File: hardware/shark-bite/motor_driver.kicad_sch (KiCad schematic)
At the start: 35 parts, among them J4 Conn_01x02_Male-Connector, U10 IRFH7440TRPBF, U11 IRFH7440TRPBF, U16 IRFH7440TRPBF, U17 IRFH7440TRPBF, U22 AOZ1282CI, U25 GD32E230G6U6TR, U28 FD6288Q, U4 IRFH7440TRPBF, U7 IRFH7440TRPBF

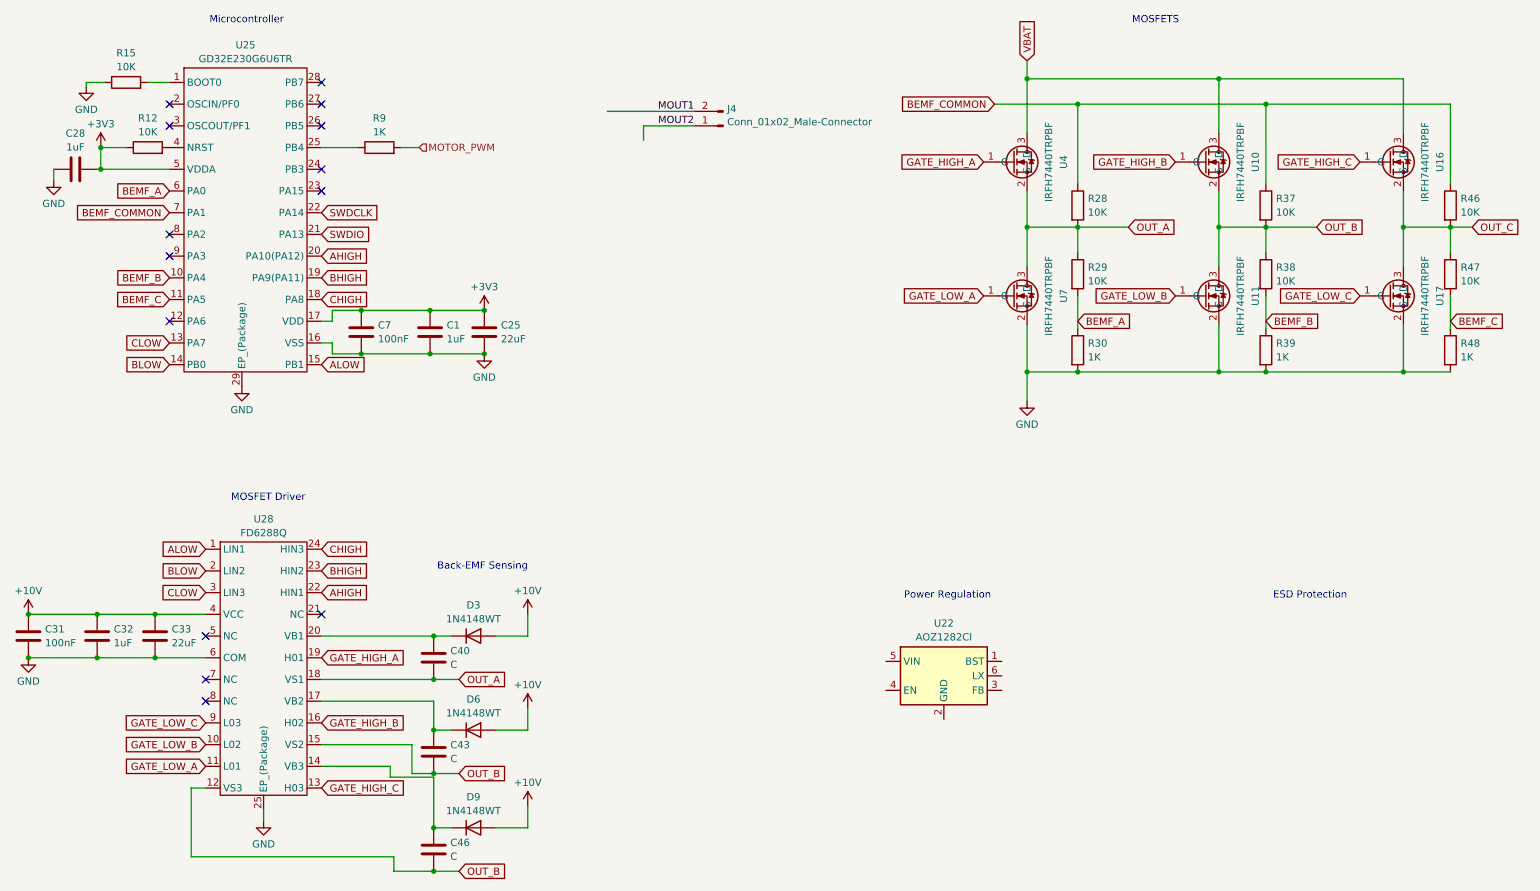
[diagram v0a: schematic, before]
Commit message: Added TVS Diodes
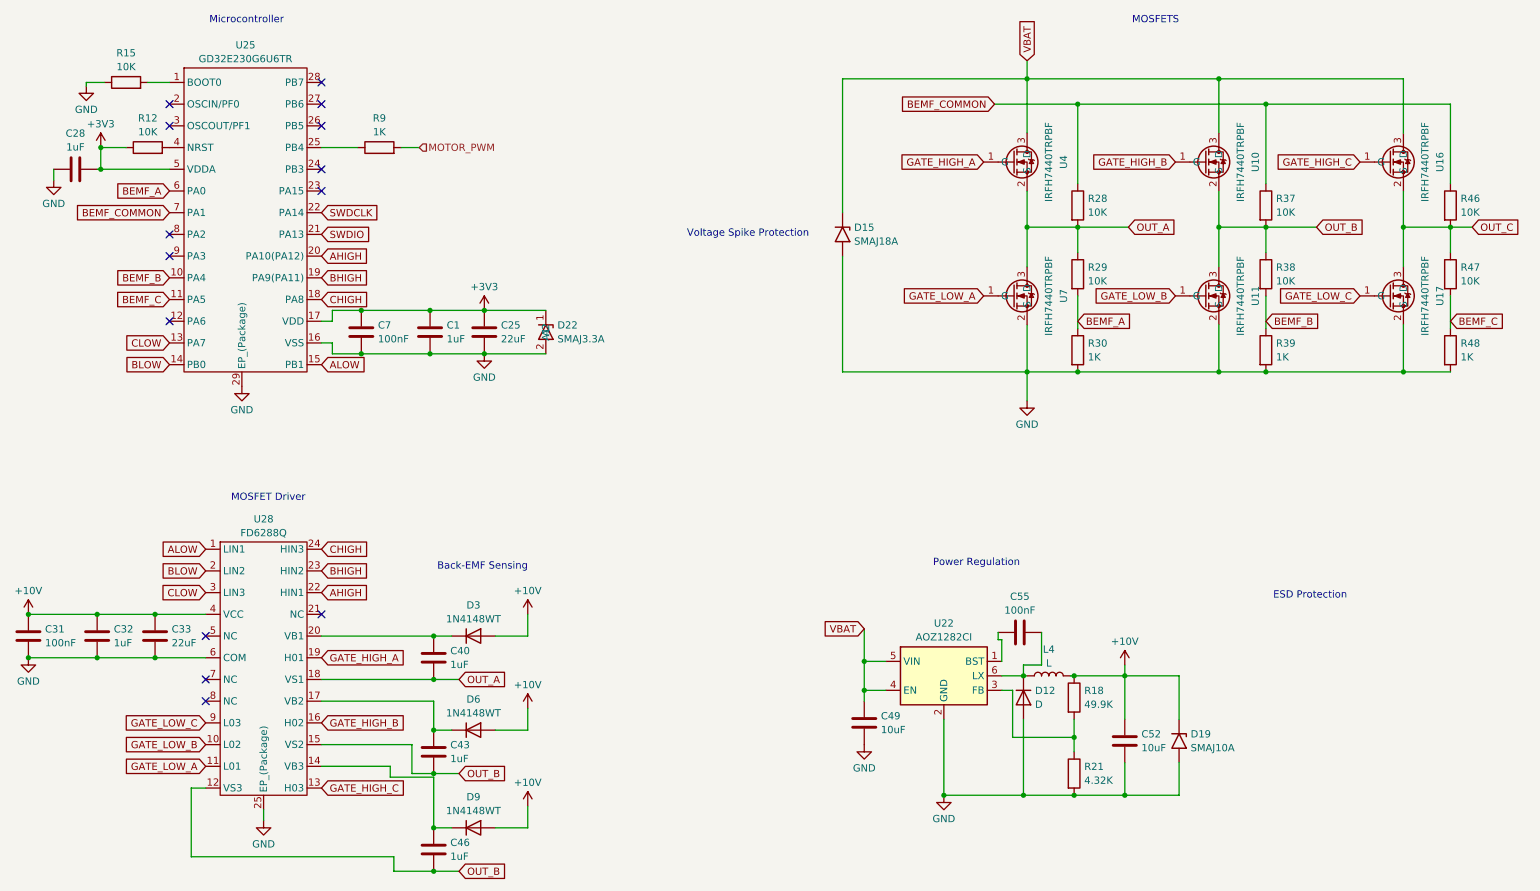
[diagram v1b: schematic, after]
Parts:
- removed J4: Conn_01x02_Male-Connector, malenki-nano:PinHeader_1x02_P2.54mm_BIG1, symbol malenki-nano-rescue:Conn_01x02_Male-Connector
- added C49, C52: 10uF, symbol Device:C
- added C55: 100nF, symbol Device:C
- added D12: D, symbol Device:D
- added D15: SMAJ18A, Diode_SMD:D_SMA, symbol Diode:SMAJ18A
- added D19: SMAJ10A, Diode_SMD:D_SMA, symbol Diode:SMAJ10A
- added D22: SMAJ3.3A, Diode_SMD:D_SMA, symbol Sharkbite:BORN_SMAJ3.3A
- added L4: L, symbol Device:L
- added R18: 49.9K, symbol Device:R
- added R21: 4.32K, symbol Device:R
- C40, C43, C46: value C -> 1uF
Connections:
- net +10V: now also C52.1, D19.1 (A1), L4.2, R18.1
- net +3V3: now also D22.1 (A1)
- net GND: now also U22.2 (GND), C49.2, C52.2, D12.2 (A), D15.2 (A2), D19.2 (A2), D22.2 (A2), R21.2
- net VBAT: now also U22.4 (EN), U22.5 (VIN), C49.1, D15.1 (A1)
- net at U22.1 (BST): now also C55.1
- net at U22.3 (FB): now also R18.2, R21.1
- net at U22.6 (LX): now also C55.2, D12.1 (K), L4.1
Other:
- note added: "Voltage Spike Protection"

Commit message: Removed Extra Diodes
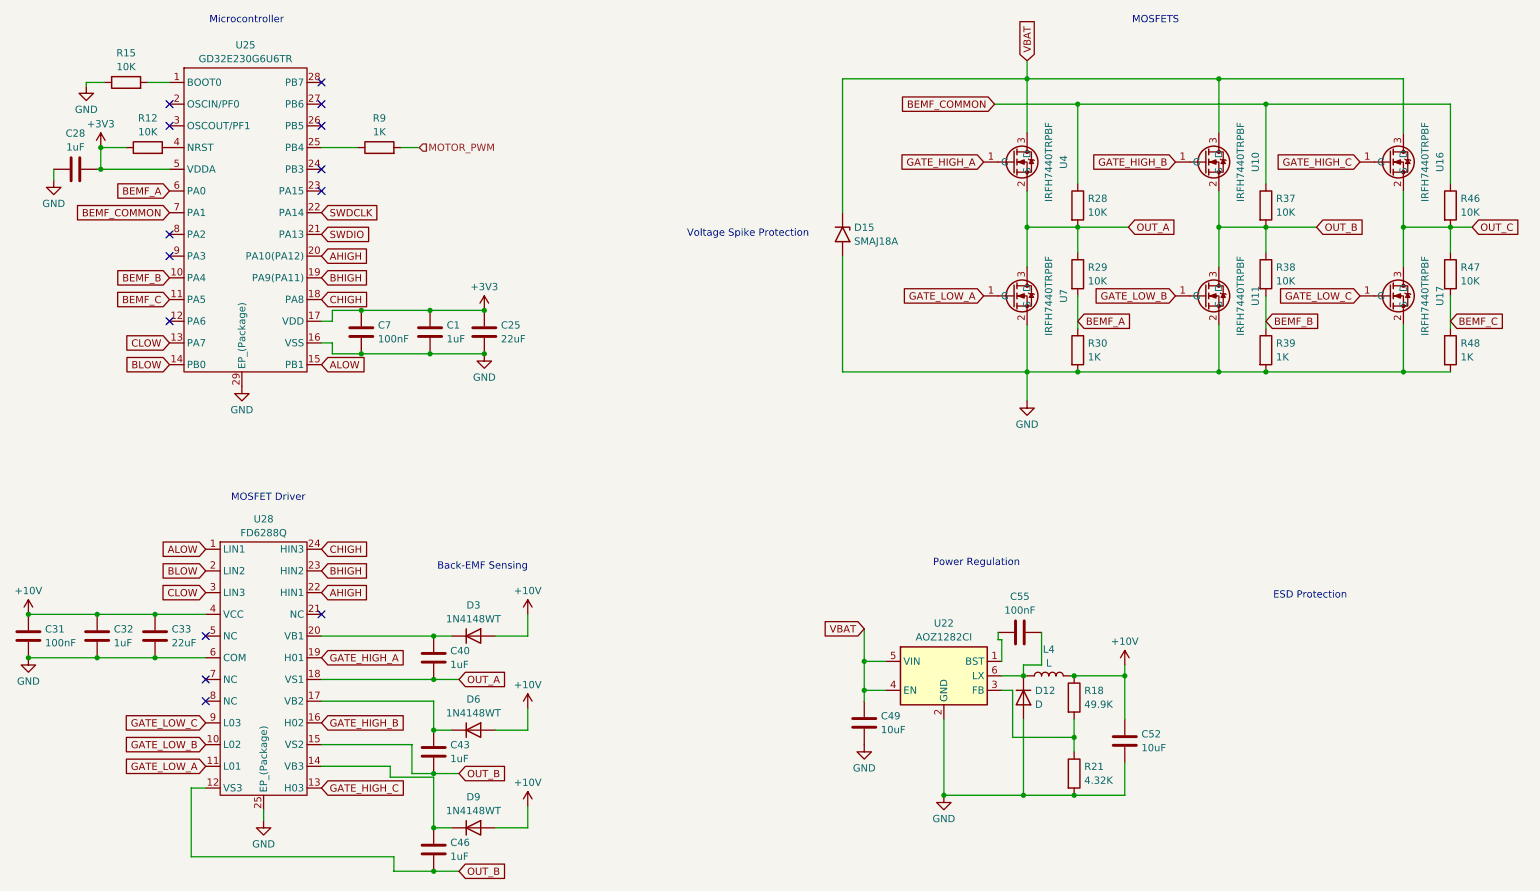
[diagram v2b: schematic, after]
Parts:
- removed D19: SMAJ10A, Diode_SMD:D_SMA, symbol Diode:SMAJ10A
- removed D22: SMAJ3.3A, Diode_SMD:D_SMA, symbol Sharkbite:BORN_SMAJ3.3A
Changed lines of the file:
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@@
   (junction (at 17.78 124.46) (diameter 0) (color 0 0 0 0)
-  )
-  (junction (at 210.185 156.21) (diameter 0) (color 0 0 0 0)
   )
   (junction (at 201.93 56.515) (diameter 0) (color 0 0 0 0)
@@
     (stroke (width 0) (type default))
   )
-  (wire (pts (xy 219.71 156.21) (xy 210.185 156.21))
-    (stroke (width 0) (type default))
-  )
   (wire (pts (xy 210.185 156.21) (xy 210.185 150.495))
     (stroke (width 0) (type default))
@@
     (stroke (width 0) (type default))
   )
-  (wire (pts (xy 219.71 142.875) (xy 219.71 135.255))
-    (stroke (width 0) (type default))
-  )
   (wire (pts (xy 88.265 78.74) (xy 97.79 78.74))
     (stroke (width 0) (type default))
@@
     (stroke (width 0) (type default))
   )
-  (wire (pts (xy 108.585 71.12) (xy 97.79 71.12))
-    (stroke (width 0) (type default))
-  )
   (wire (pts (xy 190.5 137.795) (xy 188.595 137.795))
     (stroke (width 0) (type default))
@@
     (stroke (width 0) (type default))
   )
-  (wire (pts (xy 219.71 150.495) (xy 219.71 156.21))
-    (stroke (width 0) (type default))
-  )
   (wire (pts (xy 31.115 31.115) (xy 27.94 31.115))
     (stroke (width 0) (type default))
@@
     (stroke (width 0) (type default))
   )
-  (wire (pts (xy 219.71 135.255) (xy 210.185 135.255))
-    (stroke (width 0) (type default))
-  )
   (wire (pts (xy 105.41 140.97) (xy 105.41 144.78))
     (stroke (width 0) (type default))
@@
   )
   (wire (pts (xy 201.93 34.925) (xy 234.95 34.925))
-    (stroke (width 0) (type default))
-  )
-  (wire (pts (xy 108.585 78.74) (xy 97.79 78.74))
     (stroke (width 0) (type default))
   )
@@
         (path "/f41619e3-8cf2-4511-8a51-762d4de43197/ed035ea4-687d-4ec6-a6e6-057c20ae2a22"
           (reference "R36") (unit 1)
-        )
-      )
-    )
-  )
-  (symbol (lib_id "Diode:SMAJ10A") (at 219.71 146.685 270) (unit 1)
-    (in_bom yes) (on_board yes) (dnp no) (fields_autoplaced)
-    (property "Reference" "D19" (at 221.742 145.4729 90)
-      (effects (font (size 1.27 1.27)) (justify left))
-    )
-    (property "Value" "SMAJ10A" (at 221.742 147.8971 90)
-      (effects (font (size 1.27 1.27)) (justify left))
-    )
-    (property "Footprint" "Diode_SMD:D_SMA" (at 214.63 146.685 0)
-      (effects (font (size 1.27 1.27)) hide)
-    )
-    (property "Datasheet" "https://www.littelfuse.com/media?resourcetype=datasheets&itemid=75e32973-b177-4ee3-a0ff-cedaf1abdb93&filename=smaj-datasheet" (at 219.71 145.415 0)
-      (effects (font (size 1.27 1.27)) hide)
-    )
-    (pin "1")
-    (pin "2")
-    (instances
-      (project "malenki-hv"
-        (path "/f41619e3-8cf2-4511-8a51-762d4de43197/b339fba4-a8e4-4c66-ad9c-610bd968ae93"
-          (reference "D19") (unit 1)
-        )
-        (path "/f41619e3-8cf2-4511-8a51-762d4de43197/159e78dd-19f3-45d1-a83d-5b1f96539c1f"
-          (reference "D20") (unit 1)
-        )
-        (path "/f41619e3-8cf2-4511-8a51-762d4de43197/ed035ea4-687d-4ec6-a6e6-057c20ae2a22"
-          (reference "D21") (unit 1)
         )
       )
@@
         )
       )
-    )
-  )
-  (symbol (lib_id "Sharkbite:BORN_SMAJ3.3A") (at 111.125 74.93 270) (unit 1)
-    (in_bom yes) (on_board yes) (dnp no) (fields_autoplaced)
-    (property "Reference" "D22" (at 110.617 73.7179 90)
-      (effects (font (size 1.27 1.27)) (justify left))
-    )
-    (property "Value" "SMAJ3.3A" (at 110.617 76.1421 90)
-      (effects (font (size 1.27 1.27)) (justify left))
-    )
-    (property "Footprint" "Diode_SMD:D_SMA" (at 111.125 74.93 0)
-      (effects (font (size 1.27 1.27)) hide)
-    )
-    (property "Datasheet" "https://www.lcsc.com/datasheet/lcsc_datasheet_2309251426_BORN-SMAJ3-3A_C18199544.pdf" (at 111.125 74.93 0)
-      (effects (font (size 1.27 1.27)) hide)
-    )
-    (pin "1")
-    (pin "2")
-    (instances
-      (project "malenki-hv"
-        (path "/f41619e3-8cf2-4511-8a51-762d4de43197/b339fba4-a8e4-4c66-ad9c-610bd968ae93"
-          (reference "D22") (unit 1)
-        )
-        (path "/f41619e3-8cf2-4511-8a51-762d4de43197/159e78dd-19f3-45d1-a83d-5b1f96539c1f"
-          (reference "D23") (unit 1)
-        )
-        (path "/f41619e3-8cf2-4511-8a51-762d4de43197/ed035ea4-687d-4ec6-a6e6-057c20ae2a22"
-          (reference "D24") (unit 1)
-        )
-      )
